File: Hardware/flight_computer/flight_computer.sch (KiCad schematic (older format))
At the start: 38 parts, among them J1 Micro_USB, J2 MicroSD_molex, J3 rpi_zero_w, Q1 PMOS_20V_.76A, Q2 PMOS_20V_.76A, U1 FRAM_128K, U2 STM32F427VITx, U3 MCP131T-300E_TT, Y1 Crystal_24MHZ

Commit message: Removes buzzer and adds LED pins
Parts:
- removed BZ1: Buzzer, drone_footprints:PT-2040PQ, symbol openDrone_parts:Buzzer
- removed L1: L_55m, drone_footprints:RLB0913-563K, symbol openDrone_parts:L_55m
- removed Q1: PMOS_20V_.76A, drone_footprints:NTA4151PT1G, symbol openDrone_parts:PMOS_20V_.76A
- removed R10: R_120, Resistors_SMD:R_0805, symbol openDrone_parts:R_120
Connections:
- net labels added: DEBUG_LED_1, DEBUG_LED_2, RGB_LED
- net labels removed: BUZZER_CTRL
- wire segments 159 -> 153
- no-connect marks 24 -> 22
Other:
- note removed: "BUZZER"
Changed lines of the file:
@@
 	-1   0    0    1
 $EndComp
-$Comp
-L openDrone_parts:Buzzer BZ?
-U 1 1 5FB34C23
-P 11050 10550
-AR Path="/5F5F0393/5FB34C23" Ref="BZ?"  Part="1"
-AR Path="/5FB34C23" Ref="BZ1"  Part="1"
-F 0 "BZ1" H 11202 10579 50  0000 L CNN
-F 1 "Buzzer" H 11202 10488 50  0000 L CNN
-F 2 "drone_footprints:PT-2040PQ" H 11400 11000 50  0001 C CNN
-F 3 "~" V 11025 10650 50  0001 C CNN
-F 4 "458-1078-ND" H 11350 10800 50  0001 C CNN "DPN"
-F 5 "PT-2040PQ" H 11300 10900 50  0001 C CNN "MPN"
-	1    11050 10550
-	1    0    0    -1
-$EndComp
-$Comp
-L openDrone_parts:PMOS_20V_.76A Q1
-U 1 1 5FB3B5E7
-P 10550 10550
-F 0 "Q1" H 10450 10400 50  0000 L CNN
-F 1 "PMOS_20V_.76A" H 10000 10750 50  0000 L CNN
-F 2 "drone_footprints:NTA4151PT1G" H 10000 10850 50  0001 C CNN
-F 3 "" H 10550 10550 50  0001 C CNN
-F 4 "NTA4151PT1GOSCT-ND" H 10050 10750 50  0001 C CNN "DPN"
-F 5 "NTA4151PT1G" H 9900 10650 50  0001 C CNN "MPN"
-	1    10550 10550
-	1    0    0    1
-$EndComp
-Wire Wire Line
-	10650 10350 10950 10350
-Wire Wire Line
-	10950 10350 10950 10450
-Wire Wire Line
-	10650 10750 10950 10750
-Wire Wire Line
-	10950 10750 10950 10650
-$Comp
-L openDrone_parts:L_55m L1
-U 1 1 5FB4F48A
-P 10950 9900
-F 0 "L1" H 11002 9946 50  0000 L CNN
-F 1 "L_55m" H 11002 9855 50  0000 L CNN
-F 2 "drone_footprints:RLB0913-563K" H 11750 10000 50  0001 C CNN
-F 3 "~" H 10950 9900 50  0001 C CNN
-F 4 "RLB0913-563K-ND" H 11400 10200 50  0001 C CNN "DPN"
-F 5 "RLB0913-563K" H 11350 10100 50  0001 C CNN "MPN"
-	1    10950 9900
-	1    0    0    -1
-$EndComp
-Wire Wire Line
-	10950 9750 10950 9650
-Wire Wire Line
-	10950 9650 10900 9650
-$Comp
-L power:GND #PWR013
-U 1 1 5FB579ED
-P 10950 10750
-F 0 "#PWR013" H 10950 10500 50  0001 C CNN
-F 1 "GND" H 10955 10577 50  0000 C CNN
-F 2 "" H 10950 10750 50  0001 C CNN
-F 3 "" H 10950 10750 50  0001 C CNN
-	1    10950 10750
-	1    0    0    -1
-$EndComp
-Connection ~ 10950 10750
-$Comp
-L openDrone_parts:R_120 R10
-U 1 1 5FB5ED0F
-P 10950 10200
-F 0 "R10" V 10904 10270 50  0000 L CNN
-F 1 "R_120" V 10995 10270 50  0000 L CNN
-F 2 "Resistors_SMD:R_0805" H 10150 10350 50  0001 C CNN
-F 3 "" H 10650 10700 50  0001 C CNN
-F 4 "A129738CT-ND" H 10300 10450 60  0001 C CNN "DPN"
-	1    10950 10200
-	0    1    1    0
-$EndComp
-Connection ~ 10950 10350
-Text Notes 10700 11050 0    79   ~ 0
-BUZZER
-Wire Notes Line
-	11550 11100 11550 9550
-Wire Notes Line
-	11550 9550 9950 9550
-Wire Notes Line
-	9950 9550 9950 11100
-Wire Notes Line
-	9950 11100 11550 11100
 Text Notes 700  11000 0    79   ~ 0
 BATTERY = VBAT\nBUCK CONVERTER OUTPUT (VDD_5V_BRICK) = VDD_5V_BUCK\nUSB POWER (VBUS) = VDD_5V_USB\nRADIO 5V (VDD_5V_RECEIVER) = VDD_5V_RADIO\nGENERAL 5V (VDD_5V_IN) = VDD_5V_IN\nTELEM/FRSKY (VDD_5V_PERIPH)  = VDD_5V_AUX\nSTM POWER (FMU_VDD_3V3) =  VDD_3V3_STM\nSENSORS POWER (VDD_3V3_SENSORS) = VDD_3V3_SENSORS\nRADIO POWER  (VDD_3V3_SPEKTRUM) = VDD_3V3_RADIO\n
@@
 Text Label 6800 9900 0    50   ~ 0
 VDD_3V3_STM
-Text Label 10900 9650 2    50   ~ 0
-VDD_5V_AUX
 Text Label 1700 5100 0    50   ~ 0
 VDD_5V_AUX
@@
 Text Notes 2100 1400 0    50   ~ 0
 VBAT comes in from ESC
-Text Label 10350 10550 1    50   ~ 0
-BUZZER_CTRL
-Text Label 8750 4000 0    50   ~ 0
-BUZZER_CTRL
 Text Label 1700 3450 0    50   ~ 0
 VDD_5V_RADIO
@@
 NoConn ~ 8750 5200
 NoConn ~ 8750 5300
-NoConn ~ 8750 4100
-NoConn ~ 8750 4200
 NoConn ~ 8750 4300
 NoConn ~ 8750 4400
@@
 Text Label 4400 8550 2    50   ~ 0
 OTG_FS_D_N
+Text Label 8750 4000 0    50   ~ 0
+DEBUG_LED_1
+Text Label 8750 4100 0    50   ~ 0
+DEBUG_LED_2
+Text Label 8750 4200 0    50   ~ 0
+RGB_LED
 $EndSCHEMATC

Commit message: Wires rpi, gps, and telem
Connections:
- net SPEKTRUM_POWER_CTRL: no longer names the net of U2.4 (PE5)
- no-connect marks 22 -> 23
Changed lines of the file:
@@
 F13 "VDD_3V3_STM" I R 1700 5750 50
 F14 "VDD_5V_AUX" I R 1700 5100 50
-F15 "SPEKTRUM_POWER_CTRL" I R 1700 6650 50
 F16 "VDD_3V3_RADIO_EN" I R 1700 6450 50
 $EndSheet
@@
 Text Label 1700 5200 0    50   ~ 0
 VDD_5V_IN
-Text Label 1700 6650 0    50   ~ 0
-SPEKTRUM_POWER_CTRL
-Text Label 6950 4500 2    50   ~ 0
-SPEKTRUM_POWER_CTRL
 Text Label 1700 6250 0    50   ~ 0
 VDD_USB_VALID
@@
 Text Label 8750 4200 0    50   ~ 0
 RGB_LED
+NoConn ~ 6950 4500
 $EndSCHEMATC

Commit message: Completes initial v1 pcb traces
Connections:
- net BARO_CS: now also U2.17 (PC2); no longer U2.77 (PA15)
- net DEBUG_LED_2: now also U2.16 (PC1); no longer U2.36 (PB1)
- net GYRO_DRDY: now also U2.18 (PC3); no longer U2.62 (PD15)
- net RGB_LED: now also U2.89 (PB3); no longer U2.37 (PB2)
- net RSSI_IN: now also U2.37 (PB2); no longer U2.16 (PC1)
- net SBUS_INV: now also U2.36 (PB1); no longer U2.7 (PC13)
- net VDD_USB_VALID: now also U2.51 (PB12); no longer U2.15 (PC0)
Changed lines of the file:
@@
 Text Label 1700 2450 0    50   ~ 0
 FMU_USART8_TX
-Text Label 8750 5800 0    50   ~ 0
+Text Label 8750 4200 0    50   ~ 0
 RSSI_IN
 Text Label 1700 2250 0    50   ~ 0
@@
 Text Label 8750 2600 0    50   ~ 0
 IMU_GYRO_CS
-Text Label 8750 3800 0    50   ~ 0
+Text Label 8750 5900 0    50   ~ 0
 BARO_CS
 Text Label 6950 4400 2    50   ~ 0
@@
 Text Label 8750 7100 0    50   ~ 0
 ACCEL_DRDY
-Text Label 6950 7200 2    50   ~ 0
+Text Label 8750 6000 0    50   ~ 0
 GYRO_DRDY
 Text Label 6950 5200 2    50   ~ 0
 MAG_DRDY
-Text Label 8750 7000 0    50   ~ 0
-SBUS_INV
 Text Label 1700 3850 0    50   ~ 0
 SBUS_INV
@@
 Text Label 1700 6250 0    50   ~ 0
 VDD_USB_VALID
-Text Label 8750 5700 0    50   ~ 0
+Text Label 8750 5200 0    50   ~ 0
 VDD_USB_VALID
 Text Label 1700 6150 0    50   ~ 0
@@
 $EndComp
 NoConn ~ 8750 7200
-NoConn ~ 8750 5900
-NoConn ~ 8750 6000
+NoConn ~ 8750 3800
+NoConn ~ 6950 7200
 NoConn ~ 8750 6100
 NoConn ~ 8750 5100
-NoConn ~ 8750 5200
+NoConn ~ 8750 5700
 NoConn ~ 8750 5300
-NoConn ~ 8750 4300
+NoConn ~ 8750 7000
 NoConn ~ 8750 4400
 NoConn ~ 6950 6400
@@
 Text Label 4400 8550 2    50   ~ 0
 OTG_FS_D_N
+Text Label 8750 5800 0    50   ~ 0
+DEBUG_LED_2
+Text Label 8750 4300 0    50   ~ 0
+RGB_LED
+NoConn ~ 6950 4500
+Text Label 8750 4100 0    50   ~ 0
+SBUS_INV
 Text Label 8750 4000 0    50   ~ 0
 DEBUG_LED_1
-Text Label 8750 4100 0    50   ~ 0
-DEBUG_LED_2
-Text Label 8750 4200 0    50   ~ 0
-RGB_LED
-NoConn ~ 6950 4500
 $EndSCHEMATC

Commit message: Adds debugging LEDs
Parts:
- added D8: LED_0805_Green, footprints:LED_0805_OEM, symbol openDrone_parts:LED_0805_Green
- added D9: LED_0805_Red, footprints:LED_0805_OEM, symbol openDrone_parts:LED_0805_Red
- added R10, R35: R_68, Resistors_SMD:R_0805, symbol openDrone_parts:R_68
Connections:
- net labels removed: RGB_LED
- wire segments 153 -> 159
- no-connect marks 23 -> 26
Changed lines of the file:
@@
 F13 "VDD_3V3_STM" I R 1700 5750 50
 F14 "VDD_5V_AUX" I R 1700 5100 50
-F16 "VDD_3V3_RADIO_EN" I R 1700 6450 50
+F15 "VDD_3V3_RADIO_EN" I R 1700 6450 50
 $EndSheet
 Connection ~ 8850 10300
@@
 NoConn ~ 8750 4400
 NoConn ~ 6950 6400
-NoConn ~ 6950 6500
-NoConn ~ 6950 6600
+NoConn ~ 8750 4000
+NoConn ~ 8750 5800
 NoConn ~ 6950 6800
 NoConn ~ 6950 6900
@@
 Text Label 4400 8550 2    50   ~ 0
 OTG_FS_D_N
-Text Label 8750 5800 0    50   ~ 0
+Text Label 6950 6600 2    50   ~ 0
 DEBUG_LED_2
-Text Label 8750 4300 0    50   ~ 0
-RGB_LED
 NoConn ~ 6950 4500
 Text Label 8750 4100 0    50   ~ 0
 SBUS_INV
-Text Label 8750 4000 0    50   ~ 0
+Text Label 6950 6500 2    50   ~ 0
 DEBUG_LED_1
+$Comp
+L openDrone_parts:LED_0805_Green D8
+U 1 1 5F8E0FD4
+P 11950 4250
+F 0 "D8" H 11943 3995 50  0000 C CNN
+F 1 "LED_0805_Green" H 11943 4086 50  0000 C CNN
+F 2 "footprints:LED_0805_OEM" H 11850 4250 50  0001 C CNN
+F 3 "http://www.osram-os.com/Graphics/XPic9/00078860_0.pdf" H 11950 4350 50  0001 C CNN
+F 4 "475-1410-1-ND" H 11950 4250 60  0001 C CNN "DPN"
+F 5 "LG R971-KN-1" H 11950 4250 60  0001 C CNN "MPN"
+F 6 "https://www.digikey.com/products/en?keywords=475-1410-1-ND" H 12350 4750 60  0001 C CNN "PurchasingLink"
+	1    11950 4250
+	-1   0    0    1
+$EndComp
+NoConn ~ 8750 4300
+Text Label 11650 4250 2    50   ~ 0
+DEBUG_LED_1
+Text Label 11650 4650 2    50   ~ 0
+DEBUG_LED_2
+$Comp
+L openDrone_parts:LED_0805_Red D9
+U 1 1 5F8F1D69
+P 11950 4650
+F 0 "D9" H 11943 4395 50  0000 C CNN
+F 1 "LED_0805_Red" H 11943 4486 50  0000 C CNN
+F 2 "footprints:LED_0805_OEM" H 11850 4650 50  0001 C CNN
+F 3 "https://www.digikey.com/en/products/detail/osram-opto-semiconductors-inc/LS-R976-NR-1/1227987?s=N4IgTCBcDaICwHYCsBaAjGBAOdKByAIiALoC%2BQA" H 11950 4750 50  0001 C CNN
+F 4 "475-1278-1-ND" H 11950 4650 60  0001 C CNN "DPN"
+F 5 "LG R976-NR-1" H 11950 4650 60  0001 C CNN "MPN"
+F 6 "https://www.digikey.com/products/en?keywords=475-1410-1-ND" H 12350 5150 60  0001 C CNN "PurchasingLink"
+	1    11950 4650
+	-1   0    0    1
+$EndComp
+Wire Wire Line
+	11800 4650 11650 4650
+Wire Wire Line
+	11800 4250 11650 4250
+Wire Wire Line
+	12100 4250 12200 4250
+Wire Wire Line
+	12100 4650 12200 4650
+$Comp
+L power:GND #PWR?
+U 1 1 5F90F0CE
+P 12650 4650
+AR Path="/5F615F42/5F90F0CE" Ref="#PWR?"  Part="1"
+AR Path="/5F90F0CE" Ref="#PWR0101"  Part="1"
+F 0 "#PWR0101" H 12650 4400 50  0001 C CNN
+F 1 "GND" H 12655 4477 50  0000 C CNN
+F 2 "" H 12650 4650 50  0001 C CNN
+F 3 "" H 12650 4650 50  0001 C CNN
+	1    12650 4650
+	1    0    0    -1
+$EndComp
+$Comp
+L power:GND #PWR?
+U 1 1 5F90FA48
+P 12650 4250
+AR Path="/5F615F42/5F90FA48" Ref="#PWR?"  Part="1"
+AR Path="/5F90FA48" Ref="#PWR0102"  Part="1"
+F 0 "#PWR0102" H 12650 4000 50  0001 C CNN
+F 1 "GND" H 12655 4077 50  0000 C CNN
+F 2 "" H 12650 4250 50  0001 C CNN
+F 3 "" H 12650 4250 50  0001 C CNN
+	1    12650 4250
+	1    0    0    -1
+$EndComp
+Wire Wire Line
+	12650 4250 12500 4250
+Wire Wire Line
+	12650 4650 12500 4650
+$Comp
+L openDrone_parts:R_68 R10
+U 1 1 5F920A70
+P 12350 4250
+F 0 "R10" H 12350 4457 50  0000 C CNN
+F 1 "R_68" H 12350 4366 50  0000 C CNN
+F 2 "Resistors_SMD:R_0805" H 11550 4400 50  0001 C CNN
+F 3 "" H 12050 4750 50  0001 C CNN
+F 4 "RMCF0805JT68R0CT-ND" H 11700 4500 60  0001 C CNN "DPN"
+	1    12350 4250
+	1    0    0    -1
+$EndComp
+$Comp
+L openDrone_parts:R_68 R35
+U 1 1 5F92196F
+P 12350 4650
+F 0 "R35" H 12350 4857 50  0000 C CNN
+F 1 "R_68" H 12350 4766 50  0000 C CNN
+F 2 "Resistors_SMD:R_0805" H 11550 4800 50  0001 C CNN
+F 3 "" H 12050 5150 50  0001 C CNN
+F 4 "RMCF0805JT68R0CT-ND" H 11700 4900 60  0001 C CNN "DPN"
+	1    12350 4650
+	1    0    0    -1
+$EndComp
+NoConn ~ 8750 3100
+NoConn ~ 8750 3200
 $EndSCHEMATC

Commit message: updated LEDs
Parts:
- removed R10, R35: R_68, Resistors_SMD:R_0805, symbol openDrone_parts:R_68
- added R10, R27: R_51.1, Resistors_SMD:R_0805, symbol openDrone_parts:R_51.1
- D8, D9: footprint footprints:LED_0805_OEM -> drone_footprints:LED_0805
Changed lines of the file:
@@
 F 0 "D8" H 11943 3995 50  0000 C CNN
 F 1 "LED_0805_Green" H 11943 4086 50  0000 C CNN
-F 2 "footprints:LED_0805_OEM" H 11850 4250 50  0001 C CNN
+F 2 "drone_footprints:LED_0805" H 11850 4250 50  0001 C CNN
 F 3 "http://www.osram-os.com/Graphics/XPic9/00078860_0.pdf" H 11950 4350 50  0001 C CNN
 F 4 "475-1410-1-ND" H 11950 4250 60  0001 C CNN "DPN"
@@
 F 0 "D9" H 11943 4395 50  0000 C CNN
 F 1 "LED_0805_Red" H 11943 4486 50  0000 C CNN
-F 2 "footprints:LED_0805_OEM" H 11850 4650 50  0001 C CNN
+F 2 "drone_footprints:LED_0805" H 11850 4650 50  0001 C CNN
 F 3 "https://www.digikey.com/en/products/detail/osram-opto-semiconductors-inc/LS-R976-NR-1/1227987?s=N4IgTCBcDaICwHYCsBaAjGBAOdKByAIiALoC%2BQA" H 11950 4750 50  0001 C CNN
 F 4 "475-1278-1-ND" H 11950 4650 60  0001 C CNN "DPN"
@@
 Wire Wire Line
 	12650 4650 12500 4650
+NoConn ~ 8750 3100
+NoConn ~ 8750 3200
 $Comp
-L openDrone_parts:R_68 R10
-U 1 1 5F920A70
+L openDrone_parts:R_51.1 R10
+U 1 1 5F8ECE98
 P 12350 4250
 F 0 "R10" H 12350 4457 50  0000 C CNN
-F 1 "R_68" H 12350 4366 50  0000 C CNN
+F 1 "R_51.1" H 12350 4366 50  0000 C CNN
 F 2 "Resistors_SMD:R_0805" H 11550 4400 50  0001 C CNN
 F 3 "" H 12050 4750 50  0001 C CNN
-F 4 "RMCF0805JT68R0CT-ND" H 11700 4500 60  0001 C CNN "DPN"
+F 4 "RMCF0805FT51R1CT-ND" H 11700 4500 60  0001 C CNN "DPN"
+F 5 "RMCF0805FT51R1" H 11500 4300 50  0001 C CNN "MPN"
 	1    12350 4250
 	1    0    0    -1
 $EndComp
 $Comp
-L openDrone_parts:R_68 R35
-U 1 1 5F92196F
+L openDrone_parts:R_51.1 R27
+U 1 1 5F8ED603
 P 12350 4650
-F 0 "R35" H 12350 4857 50  0000 C CNN
-F 1 "R_68" H 12350 4766 50  0000 C CNN
+F 0 "R27" H 12350 4857 50  0000 C CNN
+F 1 "R_51.1" H 12350 4766 50  0000 C CNN
 F 2 "Resistors_SMD:R_0805" H 11550 4800 50  0001 C CNN
 F 3 "" H 12050 5150 50  0001 C CNN
-F 4 "RMCF0805JT68R0CT-ND" H 11700 4900 60  0001 C CNN "DPN"
+F 4 "RMCF0805FT51R1CT-ND" H 11700 4900 60  0001 C CNN "DPN"
+F 5 "RMCF0805FT51R1" H 11500 4700 50  0001 C CNN "MPN"
 	1    12350 4650
 	1    0    0    -1
 $EndComp
-NoConn ~ 8750 3100
-NoConn ~ 8750 3200
 $EndSCHEMATC

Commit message: added switch components, worked on layout. Sensor 3V3 unfinished.
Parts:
- added C43: C_10u, Capacitors_SMD:C_0805, symbol openDrone_parts:C_10u
- added R37: R_10K, Resistors_SMD:R_0805, symbol openDrone_parts:R_10K
- added SW1: Switch_SMT, drone_footprints:PTS645SM43SMTR92LFS, symbol openDrone_parts:Switch_SMT
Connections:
- net GND: now also C43.2, SW1.3 (B), SW1.4 (B)
- net SWITCH: now reaches U2.88 (PD7)
- net SWITCH: now also C43.1, R37.1
- new net: R37.2, SW1.1 (A), SW1.2 (A)
- no-connect marks 26 -> 56
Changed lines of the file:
@@
 NoConn ~ 8750 7000
 NoConn ~ 8750 4400
-NoConn ~ 6950 6400
 NoConn ~ 8750 4000
 NoConn ~ 8750 5800
@@
 	1    0    0    -1
 $EndComp
+$Comp
+L openDrone_parts:Switch_SMT SW1
+U 1 1 5F8FB537
+P 12400 5100
+F 0 "SW1" H 12400 5335 50  0000 C CNN
+F 1 "Switch_SMT" H 12400 5244 50  0000 C CNN
+F 2 "drone_footprints:PTS645SM43SMTR92LFS" H 12350 5350 50  0001 C CNN
+F 3 "~" H 12300 5000 50  0001 C CNN
+F 4 "CKN9112CT-ND" H 12400 5450 50  0001 C CNN "DPN"
+F 5 "PTS645SM43SMTR92 LFS" H 12400 5500 50  0001 C CNN "MPN"
+	1    12400 5100
+	1    0    0    -1
+$EndComp
+Wire Wire Line
+	12200 5150 12200 5050
+$Comp
+L power:GND #PWR057
+U 1 1 5F912FF0
+P 12750 5200
+F 0 "#PWR057" H 12750 4950 50  0001 C CNN
+F 1 "GND" H 12755 5027 50  0000 C CNN
+F 2 "" H 12750 5200 50  0001 C CNN
+F 3 "" H 12750 5200 50  0001 C CNN
+	1    12750 5200
+	1    0    0    -1
+$EndComp
+Wire Wire Line
+	12200 5050 12100 5050
+Connection ~ 12200 5050
+$Comp
+L openDrone_parts:R_10K R37
+U 1 1 5F91B7A9
+P 11950 5050
+F 0 "R37" H 11950 5257 50  0000 C CNN
+F 1 "R_10K" H 11950 5166 50  0000 C CNN
+F 2 "Resistors_SMD:R_0805" H 11150 5200 50  0001 C CNN
+F 3 "" H 11650 5550 50  0001 C CNN
+F 4 "311-10.0KCRCT-ND" H 11300 5300 60  0001 C CNN "DPN"
+	1    11950 5050
+	1    0    0    -1
+$EndComp
+$Comp
+L openDrone_parts:C_10u C43
+U 1 1 5F923AE3
+P 11800 5200
+F 0 "C43" H 11915 5246 50  0000 L CNN
+F 1 "C_10u" H 11915 5155 50  0000 L CNN
+F 2 "Capacitors_SMD:C_0805" H 11838 5050 50  0001 C CNN
+F 3 "" H 11825 5300 50  0001 C CNN
+F 4 "490-16824-1-ND" H 11800 5200 60  0001 C CNN "DPN"
+	1    11800 5200
+	1    0    0    -1
+$EndComp
+$Comp
+L power:GND #PWR013
+U 1 1 5F924D72
+P 11800 5350
+F 0 "#PWR013" H 11800 5100 50  0001 C CNN
+F 1 "GND" H 11805 5177 50  0000 C CNN
+F 2 "" H 11800 5350 50  0001 C CNN
+F 3 "" H 11800 5350 50  0001 C CNN
+	1    11800 5350
+	1    0    0    -1
+$EndComp
+Wire Wire Line
+	12600 5050 12750 5050
+Wire Wire Line
+	12750 5050 12750 5150
+Wire Wire Line
+	12600 5150 12750 5150
+Connection ~ 12750 5150
+Wire Wire Line
+	12750 5150 12750 5200
+Wire Wire Line
+	11800 5050 11650 5050
+Connection ~ 11800 5050
+Text Label 6950 6400 2    50   ~ 0
+SWITCH
+Text Label 11650 5050 2    50   ~ 0
+SWITCH
+NoConn ~ 4900 8450
+NoConn ~ 8750 2300
+NoConn ~ 12350 7550
+NoConn ~ 12350 7650
+NoConn ~ 12350 7800
+NoConn ~ 12350 7900
+NoConn ~ 12350 8000
+NoConn ~ 12350 8150
+NoConn ~ 12350 8250
+NoConn ~ 12350 8350
+NoConn ~ 12350 8500
+NoConn ~ 12350 8600
+NoConn ~ 12350 9000
+NoConn ~ 12350 8900
+NoConn ~ 12350 8800
+NoConn ~ 12350 8700
+NoConn ~ 13950 7550
+NoConn ~ 13950 7650
+NoConn ~ 13950 9050
+NoConn ~ 13950 8950
+NoConn ~ 13950 8800
+NoConn ~ 13950 8700
+NoConn ~ 13950 8600
+NoConn ~ 13950 8500
+NoConn ~ 13950 8400
+NoConn ~ 13950 8250
+NoConn ~ 13950 8150
+NoConn ~ 13950 8050
+NoConn ~ 13250 7150
+NoConn ~ 13350 7150
+NoConn ~ 14900 1650
 $EndSCHEMATC

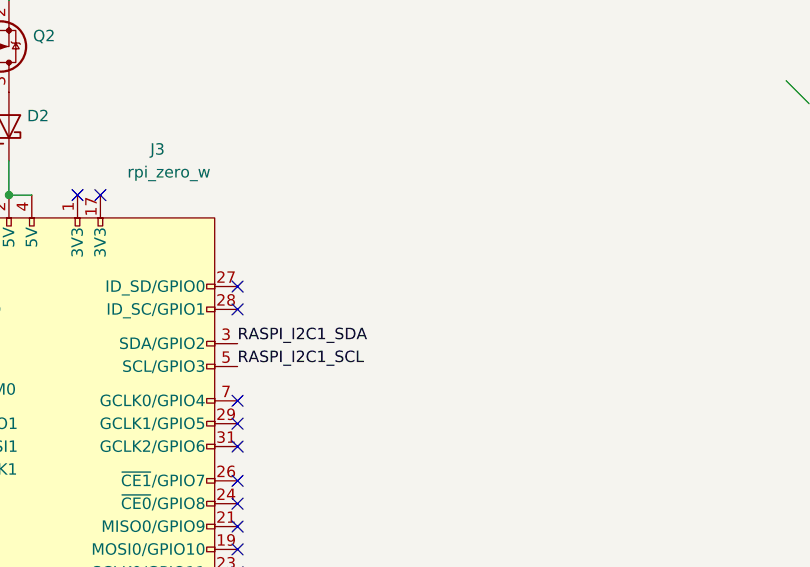
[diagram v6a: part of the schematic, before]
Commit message: Adds i2c pullup resistors
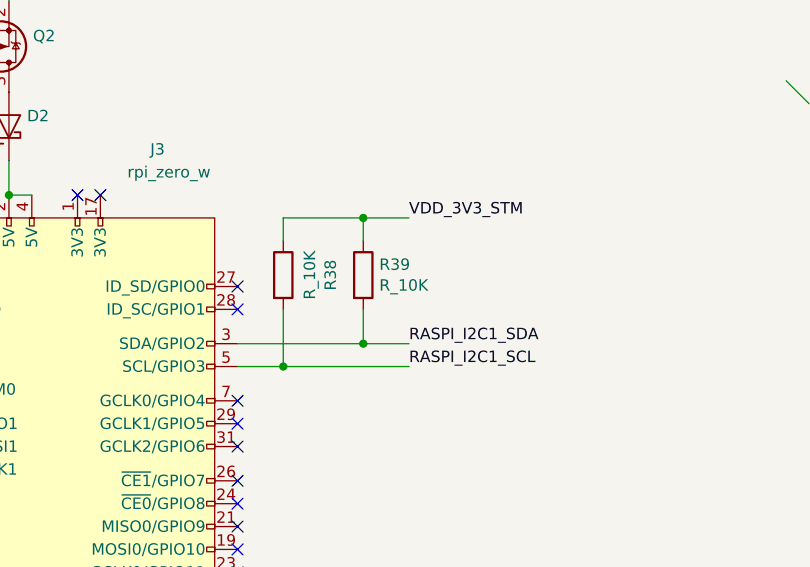
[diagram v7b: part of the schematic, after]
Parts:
- added R38, R39: R_10K, drone_footprints:R_0805, symbol openDrone_parts:R_10K
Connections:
- net RASPI_I2C1_SCL: now also R38.2
- net RASPI_I2C1_SDA: now also R39.2
- net VDD_3V3_STM: now also R38.1, R39.1
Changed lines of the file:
@@
 Text Label 8750 4900 0    50   ~ 0
 RASPI_I2C1_SDA
-Text Label 13950 7900 0    50   ~ 0
+Text Label 14700 7900 0    50   ~ 0
 RASPI_I2C1_SCL
-Text Label 13950 7800 0    50   ~ 0
+Text Label 14700 7800 0    50   ~ 0
 RASPI_I2C1_SDA
 $Comp
@@
 NoConn ~ 13350 7150
 NoConn ~ 14900 1650
+$Comp
+L openDrone_parts:R_10K R39
+U 1 1 5F9126BE
+P 14500 7500
+F 0 "R39" V 14454 7570 50  0000 L CNN
+F 1 "R_10K" V 14545 7570 50  0000 L CNN
+F 2 "drone_footprints:R_0805" H 13700 7650 50  0001 C CNN
+F 3 "" H 14200 8000 50  0001 C CNN
+F 4 "311-10.0KCRCT-ND" H 13850 7750 60  0001 C CNN "DPN"
+	1    14500 7500
+	0    1    1    0
+$EndComp
+$Comp
+L openDrone_parts:R_10K R38
+U 1 1 5F912AB7
+P 14150 7500
+F 0 "R38" H 14150 7707 50  0000 C CNN
+F 1 "R_10K" H 14150 7616 50  0000 C CNN
+F 2 "drone_footprints:R_0805" H 13350 7650 50  0001 C CNN
+F 3 "" H 13850 8000 50  0001 C CNN
+F 4 "311-10.0KCRCT-ND" H 13500 7750 60  0001 C CNN "DPN"
+	1    14150 7500
+	0    1    1    0
+$EndComp
+Text Label 14700 7250 0    50   ~ 0
+VDD_3V3_STM
+Wire Wire Line
+	14700 7250 14500 7250
+Wire Wire Line
+	14150 7250 14150 7350
+Wire Wire Line
+	14500 7350 14500 7250
+Connection ~ 14500 7250
+Wire Wire Line
+	14500 7250 14150 7250
+Wire Wire Line
+	14500 7650 14500 7800
+Wire Wire Line
+	14500 7800 14700 7800
+Wire Wire Line
+	14500 7800 13950 7800
+Connection ~ 14500 7800
+Wire Wire Line
+	14150 7650 14150 7900
+Wire Wire Line
+	14150 7900 14700 7900
+Wire Wire Line
+	14150 7900 13950 7900
+Connection ~ 14150 7900
 $EndSCHEMATC
